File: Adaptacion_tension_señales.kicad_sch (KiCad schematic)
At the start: 5 parts

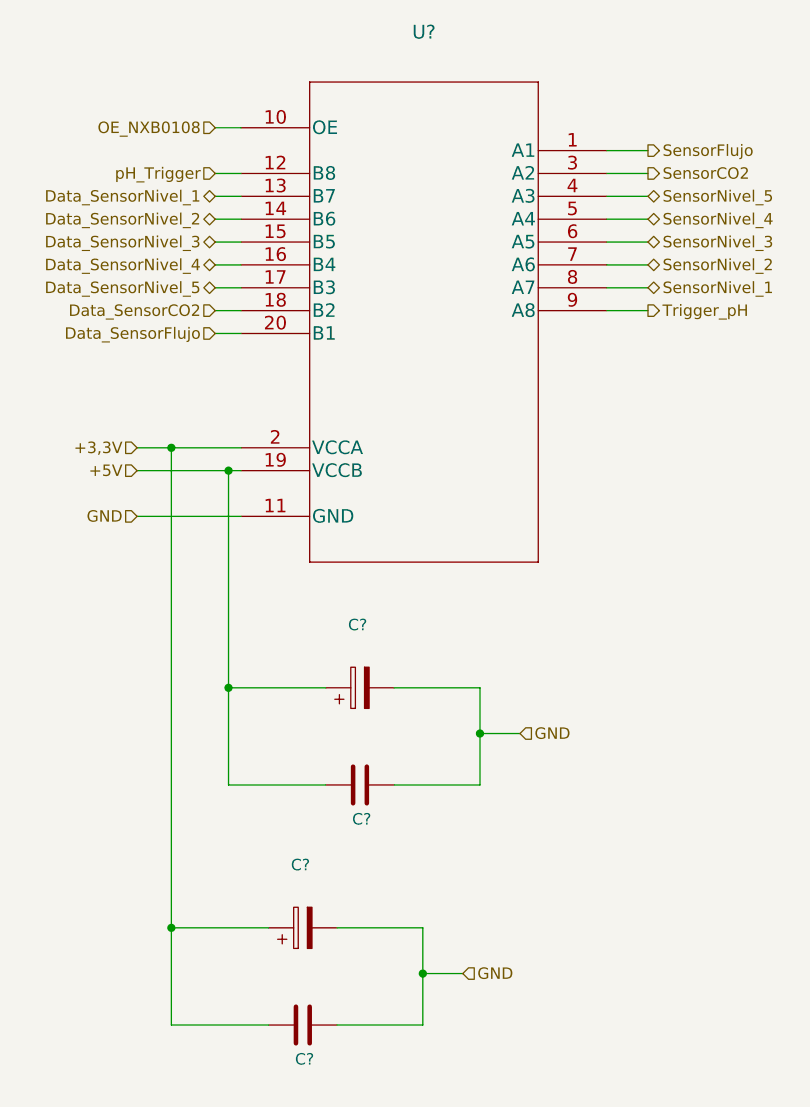
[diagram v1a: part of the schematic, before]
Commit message: Actualización de SCH según placa industrial, y búsqueda de footprints.
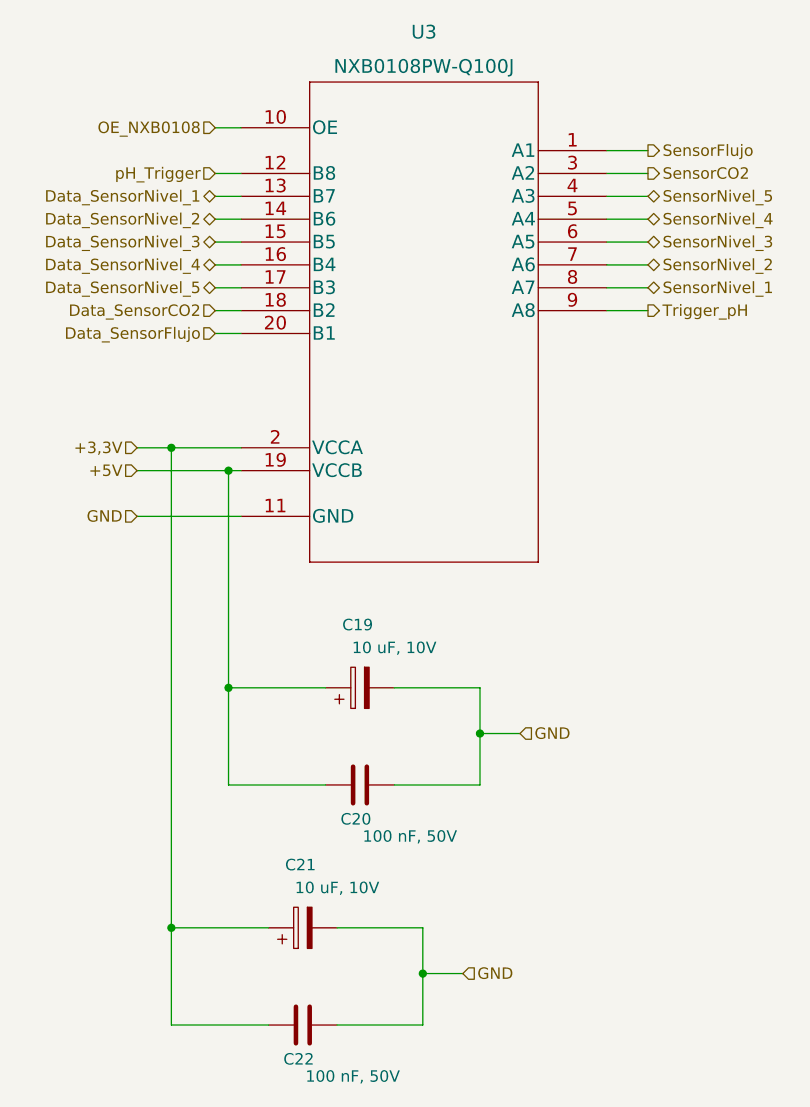
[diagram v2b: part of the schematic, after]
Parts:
- C19, C21: renamed from C?; value (none) -> 10 uF, 10V; footprint (none) -> Capacitor_SMD:C_0805_2012Metric
- C20, C22: renamed from C?; value (none) -> 100 nF, 50V; footprint (none) -> Capacitor_SMD:C_0805_2012Metric
- U3: renamed from U?; value (none) -> NXB0108PW-Q100J; footprint (none) -> Package_SO:TSSOP-20_4.4x6.5mm_P0.65mm
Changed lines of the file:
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@@
   (symbol (lib_id "Device:C") (at 132.2832 147.955 90) (unit 1)
     (in_bom yes) (on_board yes)
-    (property "Reference" "C?" (id 0) (at 133.5532 151.765 90)
+    (property "Reference" "C22" (id 0) (at 133.5532 151.765 90)
       (effects (font (size 1.27 1.27)) (justify left))
     )
-    (property "Value" "" (id 1) (at 143.0782 153.67 90)
+    (property "Value" "100 nF, 50V" (id 1) (at 143.0782 153.67 90)
       (effects (font (size 1.27 1.27)) (justify left))
     )
-    (property "Footprint" "" (id 2) (at 136.0932 146.9898 0)
+    (property "Footprint" "Capacitor_SMD:C_0805_2012Metric" (id 2) (at 136.0932 146.9898 0)
       (effects (font (size 1.27 1.27)) hide)
     )
@@
   (symbol (lib_id "Device:C") (at 138.6332 121.285 90) (unit 1)
     (in_bom yes) (on_board yes)
-    (property "Reference" "C?" (id 0) (at 139.9032 125.095 90)
+    (property "Reference" "C20" (id 0) (at 139.9032 125.095 90)
       (effects (font (size 1.27 1.27)) (justify left))
     )
-    (property "Value" "" (id 1) (at 149.4282 127 90)
+    (property "Value" "100 nF, 50V" (id 1) (at 149.4282 127 90)
       (effects (font (size 1.27 1.27)) (justify left))
     )
-    (property "Footprint" "" (id 2) (at 142.4432 120.3198 0)
+    (property "Footprint" "Capacitor_SMD:C_0805_2012Metric" (id 2) (at 142.4432 120.3198 0)
       (effects (font (size 1.27 1.27)) hide)
     )
@@
   (symbol (lib_id "Device:C_Polarized") (at 132.2832 137.16 90) (unit 1)
     (in_bom yes) (on_board yes)
-    (property "Reference" "C?" (id 0) (at 132.0292 130.175 90))
-    (property "Value" "" (id 1) (at 136.0932 132.715 90))
-    (property "Footprint" "" (id 2) (at 136.0932 136.1948 0)
+    (property "Reference" "C21" (id 0) (at 132.0292 130.175 90))
+    (property "Value" "10 uF, 10V" (id 1) (at 136.0932 132.715 90))
+    (property "Footprint" "Capacitor_SMD:C_0805_2012Metric" (id 2) (at 136.0932 136.1948 0)
       (effects (font (size 1.27 1.27)) hide)
     )
@@
   (symbol (lib_id "Device:C_Polarized") (at 138.6332 110.49 90) (unit 1)
     (in_bom yes) (on_board yes)
-    (property "Reference" "C?" (id 0) (at 138.3792 103.505 90))
-    (property "Value" "" (id 1) (at 142.4432 106.045 90))
-    (property "Footprint" "" (id 2) (at 142.4432 109.5248 0)
+    (property "Reference" "C19" (id 0) (at 138.3792 103.505 90))
+    (property "Value" "10 uF, 10V" (id 1) (at 142.4432 106.045 90))
+    (property "Footprint" "Capacitor_SMD:C_0805_2012Metric" (id 2) (at 142.4432 109.5248 0)
       (effects (font (size 1.27 1.27)) hide)
     )
@@
   (symbol (lib_id "NXB0108PWJ:NXB0108PW-Q100J") (at 125.4252 48.26 0) (unit 1)
     (in_bom yes) (on_board yes) (fields_autoplaced)
-    (property "Reference" "U?" (id 0) (at 145.7452 37.6428 0)
+    (property "Reference" "U3" (id 0) (at 145.7452 37.6428 0)
       (effects (font (size 1.524 1.524)))
     )
-    (property "Value" "" (id 1) (at 145.7452 41.4528 0)
+    (property "Value" "NXB0108PW-Q100J" (id 1) (at 145.7452 41.4528 0)
       (effects (font (size 1.524 1.524)))
     )
-    (property "Footprint" "" (id 2) (at 145.7452 42.164 0)
+    (property "Footprint" "Package_SO:TSSOP-20_4.4x6.5mm_P0.65mm" (id 2) (at 145.7452 42.164 0)
       (effects (font (size 1.524 1.524)) hide)
     )

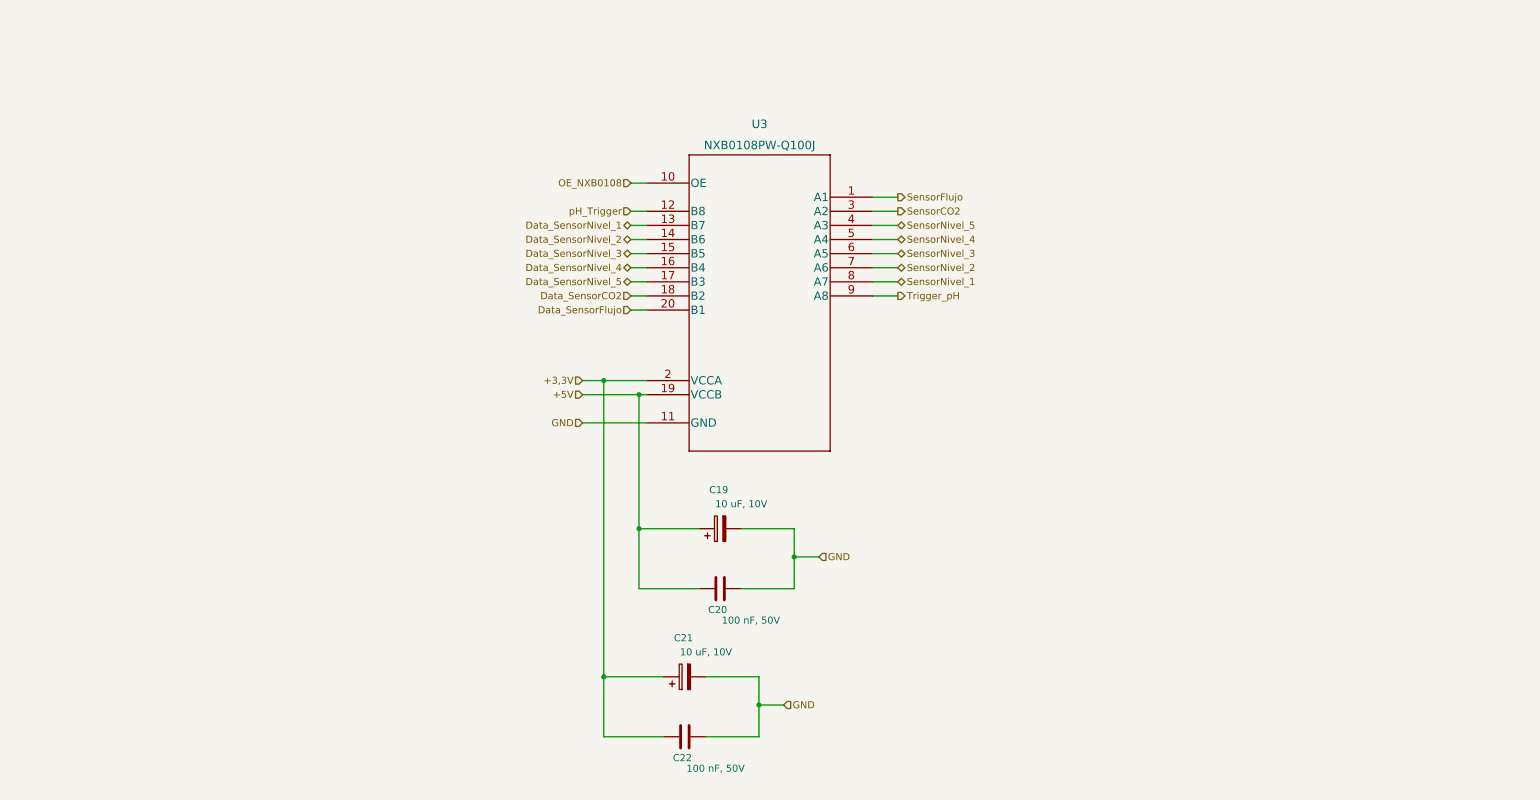
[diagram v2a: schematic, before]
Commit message: Cambios en SCH y PCB.
Se cambio el adaptador de nivel 5-3,3V por un circuito con MOSFET 2N7002, dado que ya no hay stock del NXB. Se modificó el footprint del expansor I/O por uno thorugh-hole.
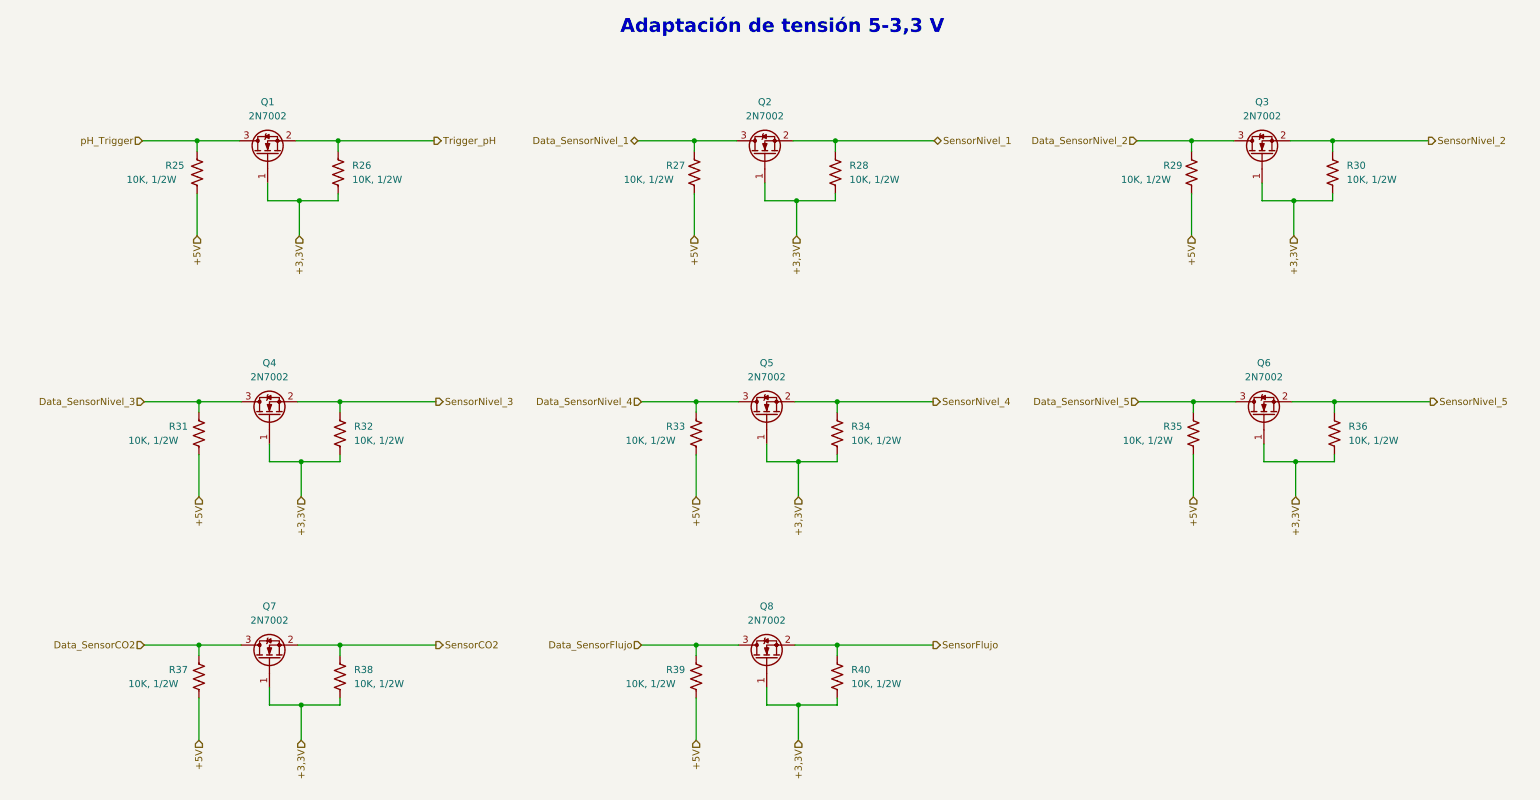
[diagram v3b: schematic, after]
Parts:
- removed C19, C21: 10 uF, 10V, Capacitor_SMD:C_0805_2012Metric, symbol Device:C_Polarized
- removed C20, C22: 100 nF, 50V, Capacitor_SMD:C_0805_2012Metric, symbol Device:C
- removed U3: NXB0108PW-Q100J, Package_SO:TSSOP-20_4.4x6.5mm_P0.65mm, symbol NXB0108PWJ:NXB0108PW-Q100J
- added Q1, Q2, Q3, Q4, Q5, Q6, Q7, Q8: 2N7002, Package_TO_SOT_SMD:SOT-23, symbol Transistor_FET:2N7002
- added R25, R26, R27, R28, R29, R30, R31, R32, R33, R34, R35, R36, R37, R38, R39, R40: 10K, 1/2W, Resistor_SMD:R_0805_2012Metric, symbol Device:R_US
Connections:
- net +3,3V: now also Q1.1 (G), Q2.1 (G), Q3.1 (G), Q4.1 (G), Q5.1 (G), Q6.1 (G), Q7.1 (G), Q8.1 (G), R26.2, R28.2, R30.2, R32.2, R34.2, R36.2, R38.2, R40.2
- net +5V: now also R25.2, R27.2, R29.2, R31.2, R33.2, R35.2, R37.2, R39.2
- net Data_SensorCO2: now also Q7.3 (D), R37.1
- net Data_SensorFlujo: now also Q8.3 (D), R39.1
- net Data_SensorNivel_1: now also Q2.3 (D), R27.1
- net Data_SensorNivel_2: now also Q3.3 (D), R29.1
- net Data_SensorNivel_3: now also Q4.3 (D), R31.1
- net Data_SensorNivel_4: now also Q5.3 (D), R33.1
- net Data_SensorNivel_5: now also Q6.3 (D), R35.1
- net SensorCO2: now also Q7.2 (S), R38.1
- net SensorFlujo: now also Q8.2 (S), R40.1
- net SensorNivel_1: now also Q2.2 (S), R28.1
- net SensorNivel_2: now also Q3.2 (S), R30.1
- net SensorNivel_3: now also Q4.2 (S), R32.1
- net SensorNivel_4: now also Q5.2 (S), R34.1
- net SensorNivel_5: now also Q6.2 (S), R36.1
- net Trigger_pH: now also Q1.2 (S), R26.1
- net pH_Trigger: now also Q1.3 (D), R25.1
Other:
- note added: "Adaptación de tensión 5-3,3 V"

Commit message: Se finalizó con el PCB del prototipo.
Dado que se buscó a toda costa que el PCB fuera de 1 capa, en varios puntos del circuito se tuvieron que agregar pin headers individuales para conectar a 3V3 y GND, junto con tiras de pin headers. Cada una de estas se conectara luego entre si mediante cables.

Tambien se generaron los archivos Gerber y BOM.
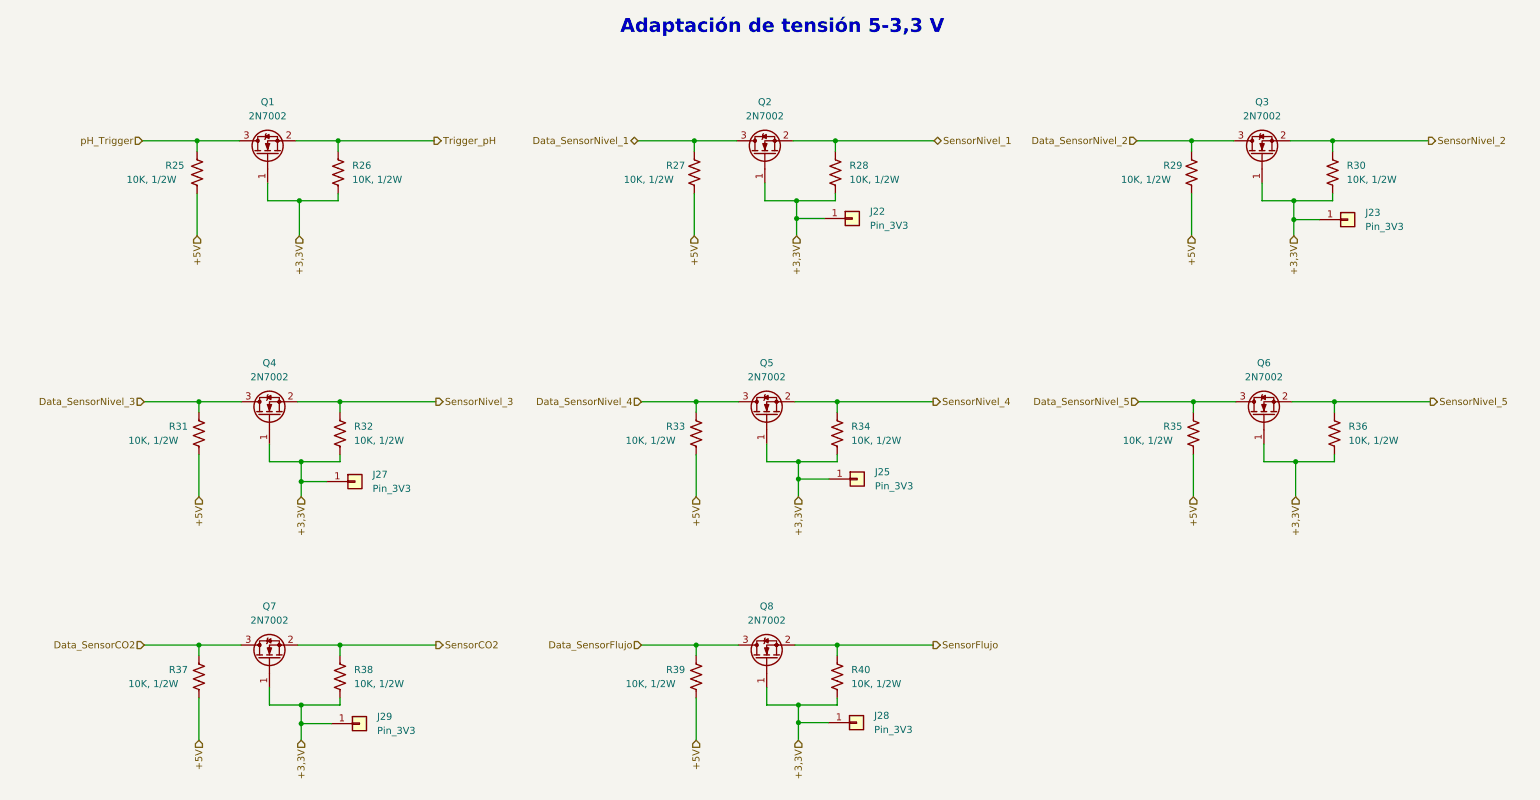
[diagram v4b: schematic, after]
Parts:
- added J22, J23, J25, J27, J28, J29: Pin_3V3, Connector_PinHeader_2.54mm:PinHeader_1x01_P2.54mm_Vertical, symbol Connector_Generic:Conn_01x01
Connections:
- net +3,3V: now also J22.1 (Pin_1), J23.1 (Pin_1), J25.1 (Pin_1), J27.1 (Pin_1), J28.1 (Pin_1), J29.1 (Pin_1)
